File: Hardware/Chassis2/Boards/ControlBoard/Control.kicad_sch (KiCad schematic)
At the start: 2 parts

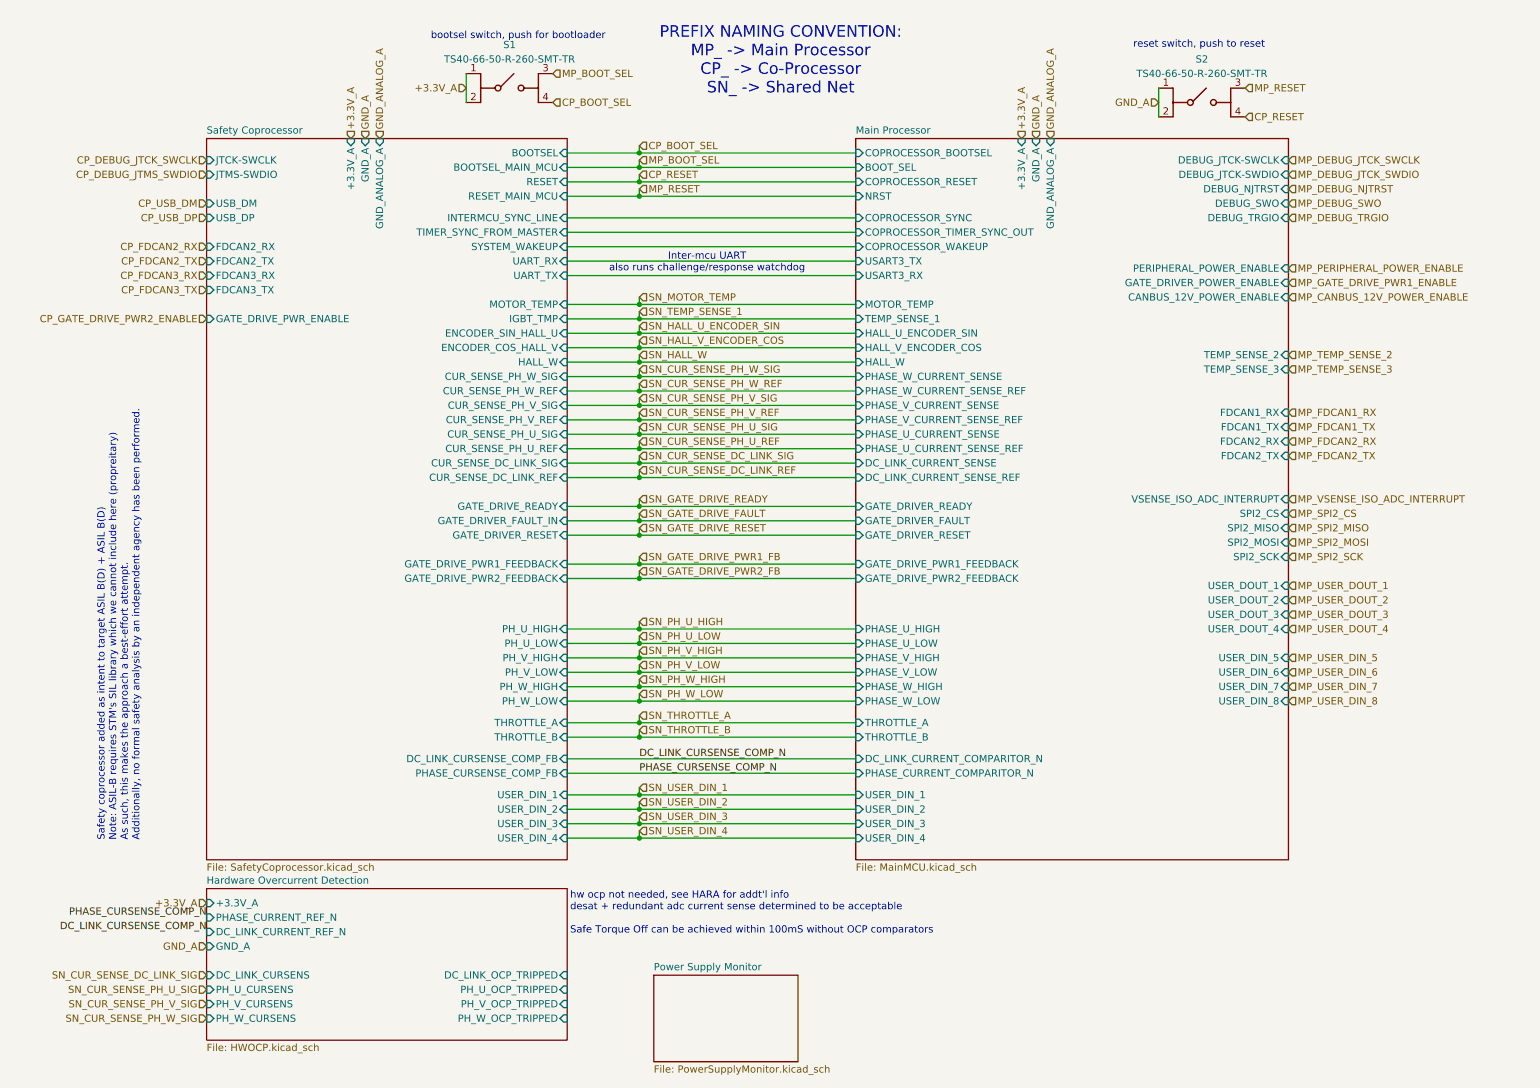
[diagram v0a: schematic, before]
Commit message: Add Schematic / Controlboard Support for Multi-Drive Mulit-Phase, DDCP
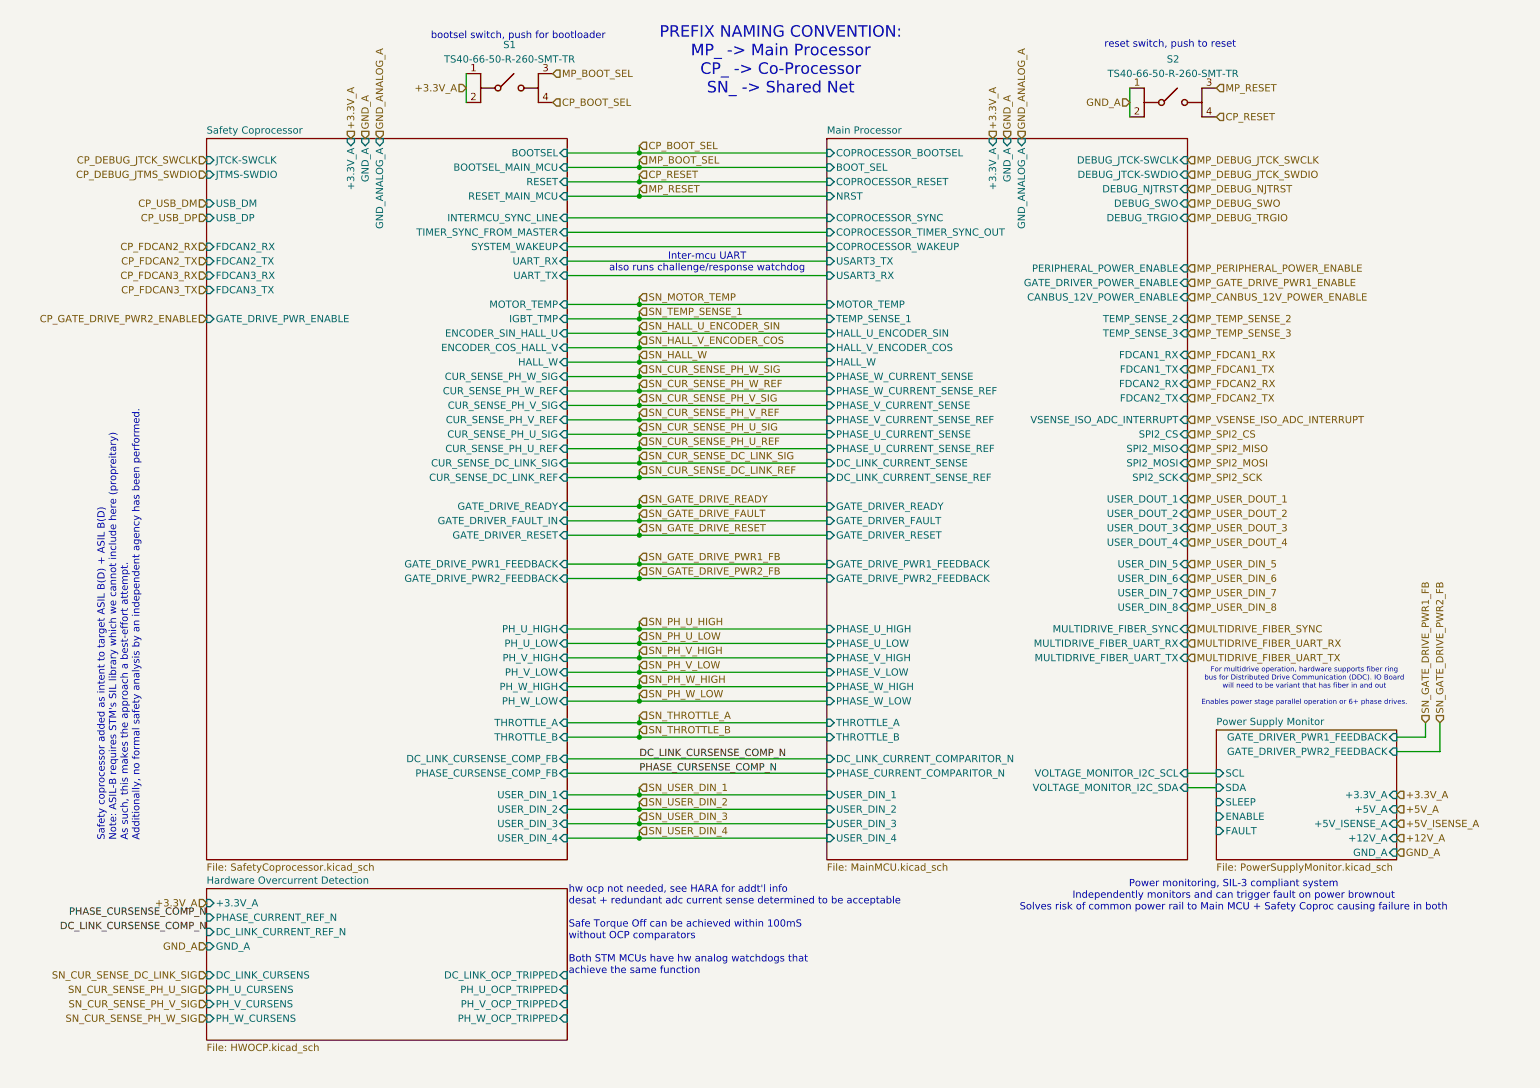
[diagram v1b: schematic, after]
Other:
- sheet Main Processor ports: added MULTIDRIVE_FIBER_SYNC, MULTIDRIVE_FIBER_UART_RX, MULTIDRIVE_FIBER_UART_TX, VOLTAGE_MONITOR_I2C_SCL, VOLTAGE_MONITOR_I2C_SDA; removed none
- sheet Power Supply Monitor ports: added +12V_A, +3.3V_A, +5V_A, +5V_ISENSE_A, ENABLE, FAULT, GATE_DRIVER_PWR1_FEEDBACK, GATE_DRIVER_PWR2_FEEDBACK, GND_A, SCL, SDA, SLEEP; removed none
- note added: "For multidrive operation, hardware supports fiber ring bus for Distributed Drive Communication (DDC). IO Board will need to be variant that has fiber in and out Enables power stage parallel operation or 6+ phase drives."
- note added: "Power monitoring, SIL-3 compliant system Independently monitors and can trigger fault on power brownout Solves risk of common power rail to Main MCU + Safety Coproc causing failure in both"
- note added: "hw ocp not needed, see HARA for addt'l info desat + redundant adc current sense determined to be acceptable Safe Torque Off can be achieved within 100mS without OCP comparators Both STM MCUs have hw analog watchdogs that achieve the same function"
- note removed: "hw ocp not needed, see HARA for addt'l info desat + redundant adc current sense determined to be acceptable Safe Torque Off can be achieved within 100mS without OCP comparators"
- moved on the sheet: S2

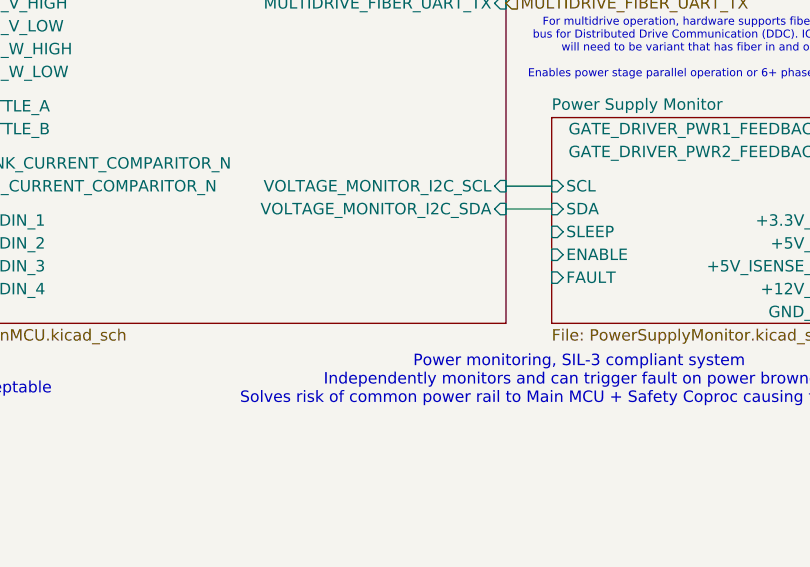
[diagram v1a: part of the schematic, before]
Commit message: fix power monitor ic connections
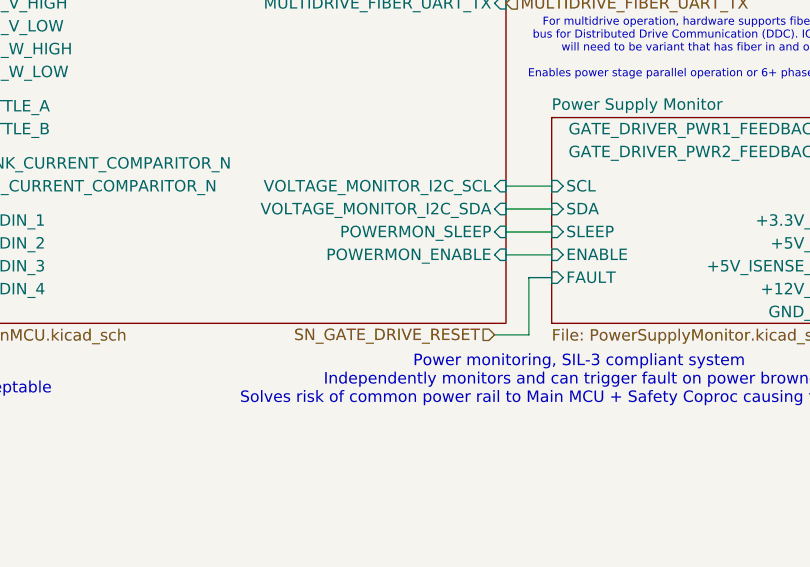
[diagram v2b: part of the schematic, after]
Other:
- sheet Main Processor ports: added POWERMON_ENABLE, POWERMON_SLEEP; removed none
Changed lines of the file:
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@@
 	(wire
 		(pts
+			(xy 218.44 157.48) (xy 220.98 157.48)
+		)
+		(stroke
+			(width 0)
+			(type default)
+		)
+	)
+	(wire
+		(pts
 			(xy 106.68 90.17) (xy 119.38 90.17)
 		)
@@
 	(wire
 		(pts
+			(xy 218.44 163.83) (xy 218.44 157.48)
+		)
+		(stroke
+			(width 0)
+			(type default)
+		)
+	)
+	(wire
+		(pts
 			(xy 119.38 71.12) (xy 119.38 72.39)
 		)
@@
 	(wire
 		(pts
+			(xy 215.9 152.4) (xy 220.98 152.4)
+		)
+		(stroke
+			(width 0)
+			(type default)
+		)
+	)
+	(wire
+		(pts
 			(xy 215.9 147.32) (xy 220.98 147.32)
 		)
@@
 	(wire
 		(pts
+			(xy 215.9 154.94) (xy 220.98 154.94)
+		)
+		(stroke
+			(width 0)
+			(type default)
+		)
+	)
+	(wire
+		(pts
 			(xy 119.38 134.62) (xy 152.4 134.62)
 		)
@@
 	(wire
 		(pts
+			(xy 214.63 163.83) (xy 218.44 163.83)
+		)
+		(stroke
+			(width 0)
+			(type default)
+		)
+	)
+	(wire
+		(pts
 			(xy 119.38 76.2) (xy 119.38 77.47)
 		)
@@
 		)
 	)
+	(hierarchical_label "SN_GATE_DRIVE_RESET"
+		(shape input)
+		(at 214.63 163.83 180)
+		(effects
+			(font
+				(size 1.27 1.27)
+			)
+			(justify right)
+		)
+	)
 	(hierarchical_label "SN_GATE_DRIVE_PWR1_FB"
 		(shape input)
@@
 			(effects
 				(font
+					(size 1.27 1.27)
+				)
+				(justify right)
+			)
+		)
+		(pin "POWERMON_ENABLE" input
+			(at 215.9 154.94 0)
+			(effects
+				(font
+					(size 1.27 1.27)
+				)
+				(justify right)
+			)
+		)
+		(pin "POWERMON_SLEEP" input
+			(at 215.9 152.4 0)
+			(effects
+				(font

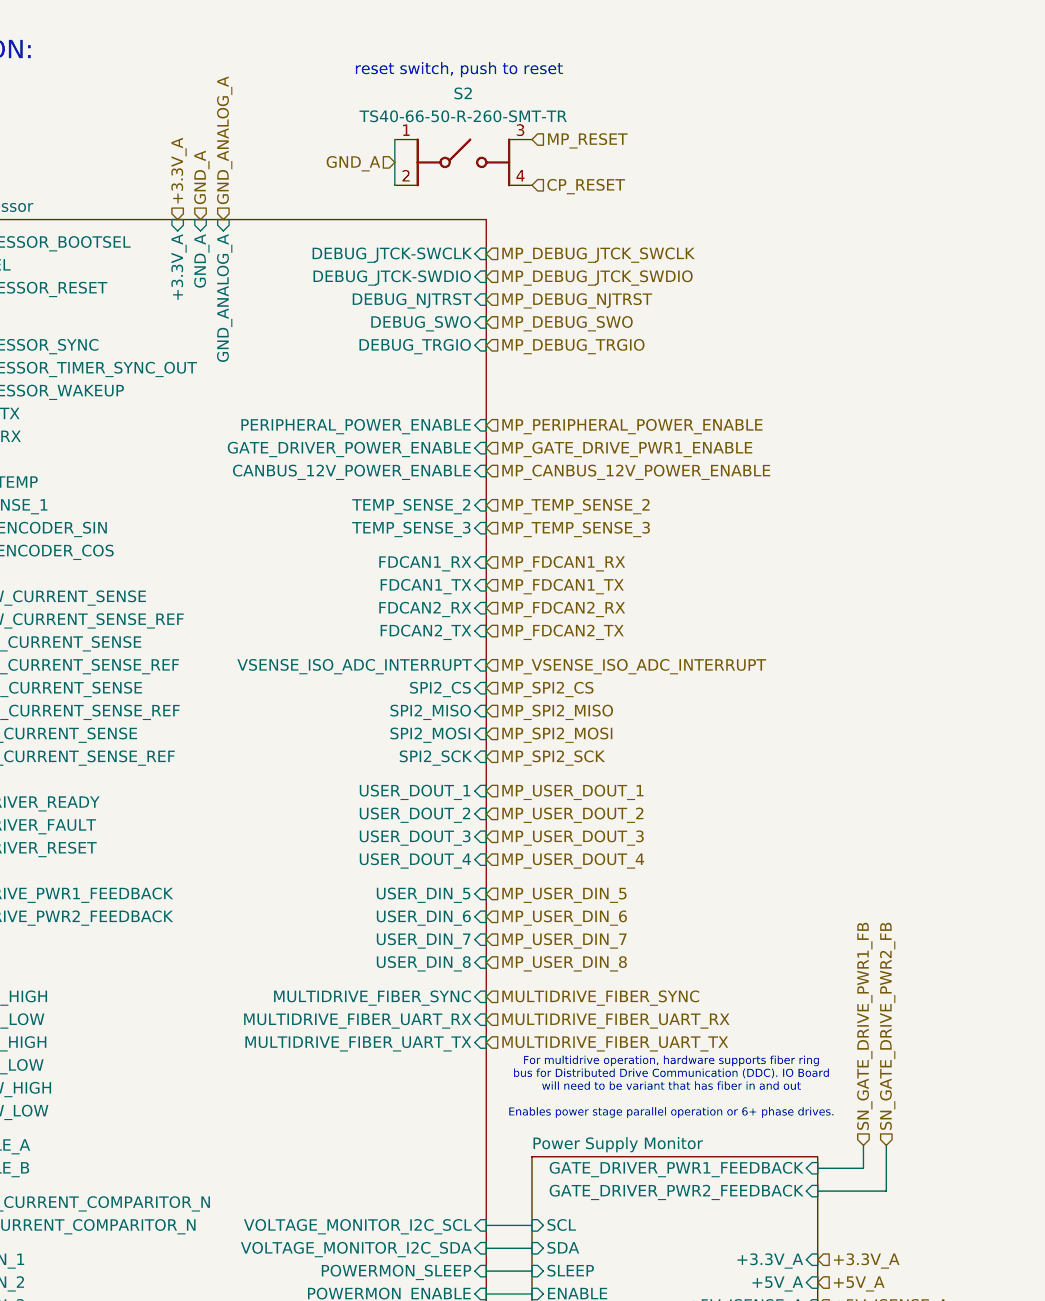
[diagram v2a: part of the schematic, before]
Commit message: Add temp sense, finish layout, tiding silkscreen for control board
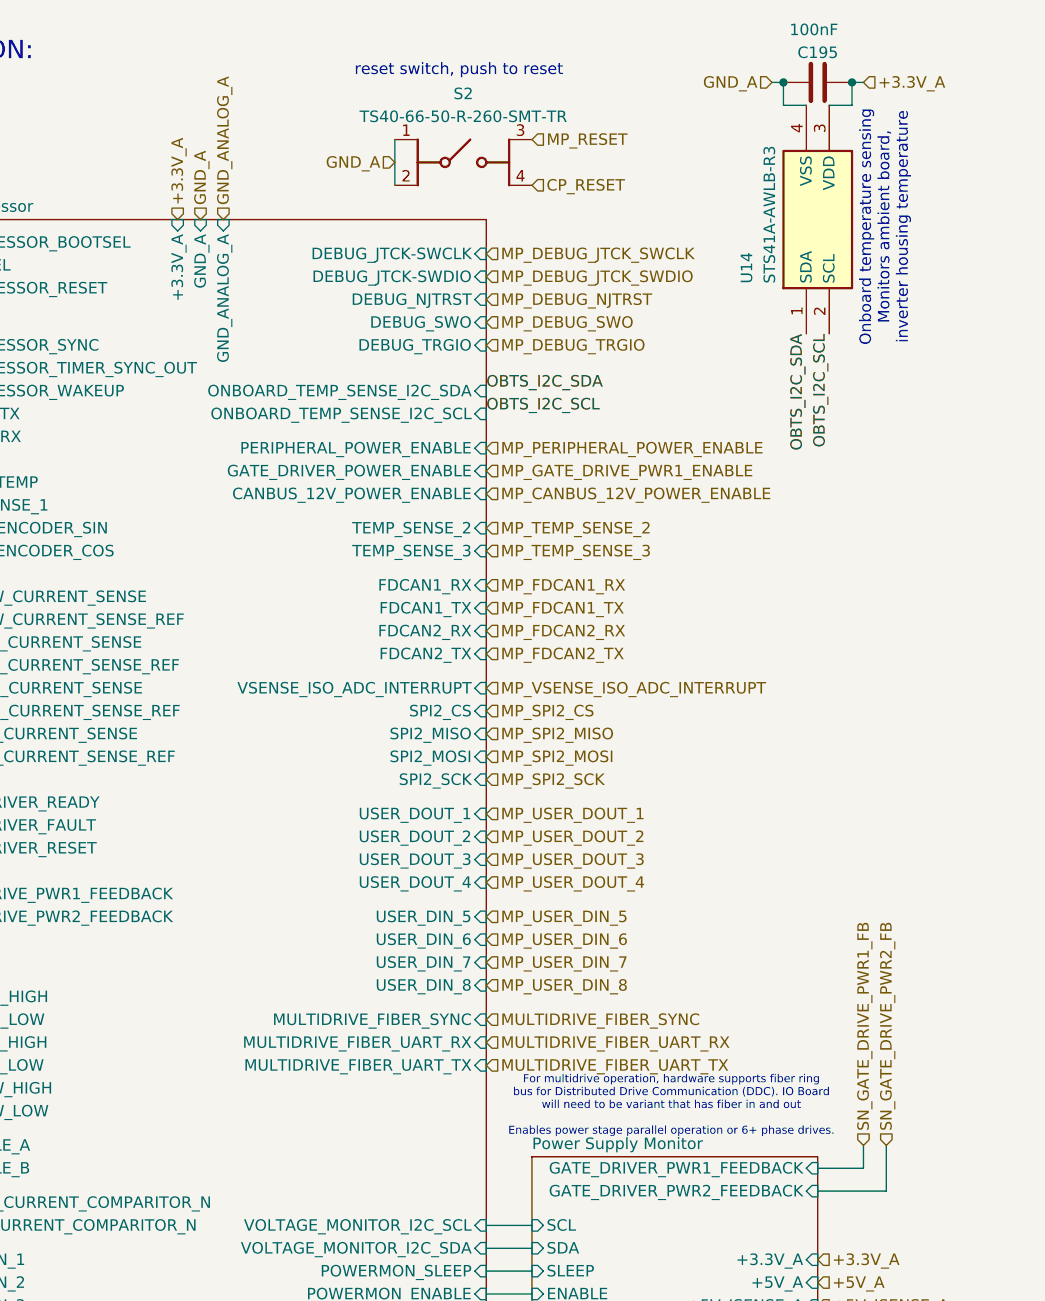
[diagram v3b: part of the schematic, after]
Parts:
- added C195: 100nF, Capacitor_SMD:C_1210_3225Metric_Pad1.33x2.70mm_HandSolder, symbol Device:C
- added U14: STS41A-AWLB-R3, STS41AAWLBR3, symbol InverterCom:STS41A-AWLB-R3
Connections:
- net +3.3V_A: now also C195.2, U14.3 (VDD)
- net GND_A: now also C195.1, U14.4 (VSS)
- new net OBTS_I2C_SCL: U14.2 (SCL)
- new net OBTS_I2C_SDA: U14.1 (SDA)
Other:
- sheet Main Processor ports: added ONBOARD_TEMP_SENSE_I2C_SCL, ONBOARD_TEMP_SENSE_I2C_SDA; removed none
- note added: "Onboard temperature sensing Monitors ambient board, inverter housing temperature"

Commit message: finalize models, parts, connectors, pn for ctrlbd
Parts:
- U14: footprint STS41AAWLBR3 -> InverterCom:STS41AAWLBR3
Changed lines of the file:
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@@
 		(title "Open Inverter Platform - Control Board")
 		(date "2026-07-07")
-		(rev "G")
+		(rev "A")
 		(company "Corzine Lab, University of California, Santa Cruz")
 		(comment 1 "Prepared by Thomas Liao")
+		(comment 2 "HW-C2-PCB-CTRL")
 	)
 	(text "hw ocp not needed, see HARA for addt'l info\ndesat + redundant adc current sense determined to be acceptable\n\nSafe Torque Off can be achieved within 100mS\nwithout OCP comparators\n\nBoth STM MCUs have hw analog watchdogs that\nachieve the same function"
@@
 			)
 		)
-		(property "Footprint" "STS41AAWLBR3"
+		(property "Footprint" "InverterCom:STS41AAWLBR3"
 			(at 346.38 26.67 0)
 			(hide yes)

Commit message: Labels tool, composite board views, InverterGen5 C2 branding, even render resolution
- Labels.pdf: HV warning labels, chassis ID, per-assembly labels (label cmd)
- Board sections add composite front/back views (PCB-viewer look, mirrored
  back) and layer plots now carry the drawing sheet with true plot scale
- Branding standardized to InverterGen5 C2 (cover, footer, labels)
- STEP previews render at even resolution regardless of part aspect
- Fab part titles from info.txt PartName; ALL-CAPS handling fixed
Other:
- title: Open Inverter Platform - Control Board -> InverterGen5 - Control Board
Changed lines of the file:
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@@
 	(paper "USLetter")
 	(title_block
-		(title "Open Inverter Platform - Control Board")
+		(title "InverterGen5 - Control Board")
 		(date "2026-07-07")
 		(rev "A")
